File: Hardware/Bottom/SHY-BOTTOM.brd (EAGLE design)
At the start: 160 x 100 mm, 0 parts

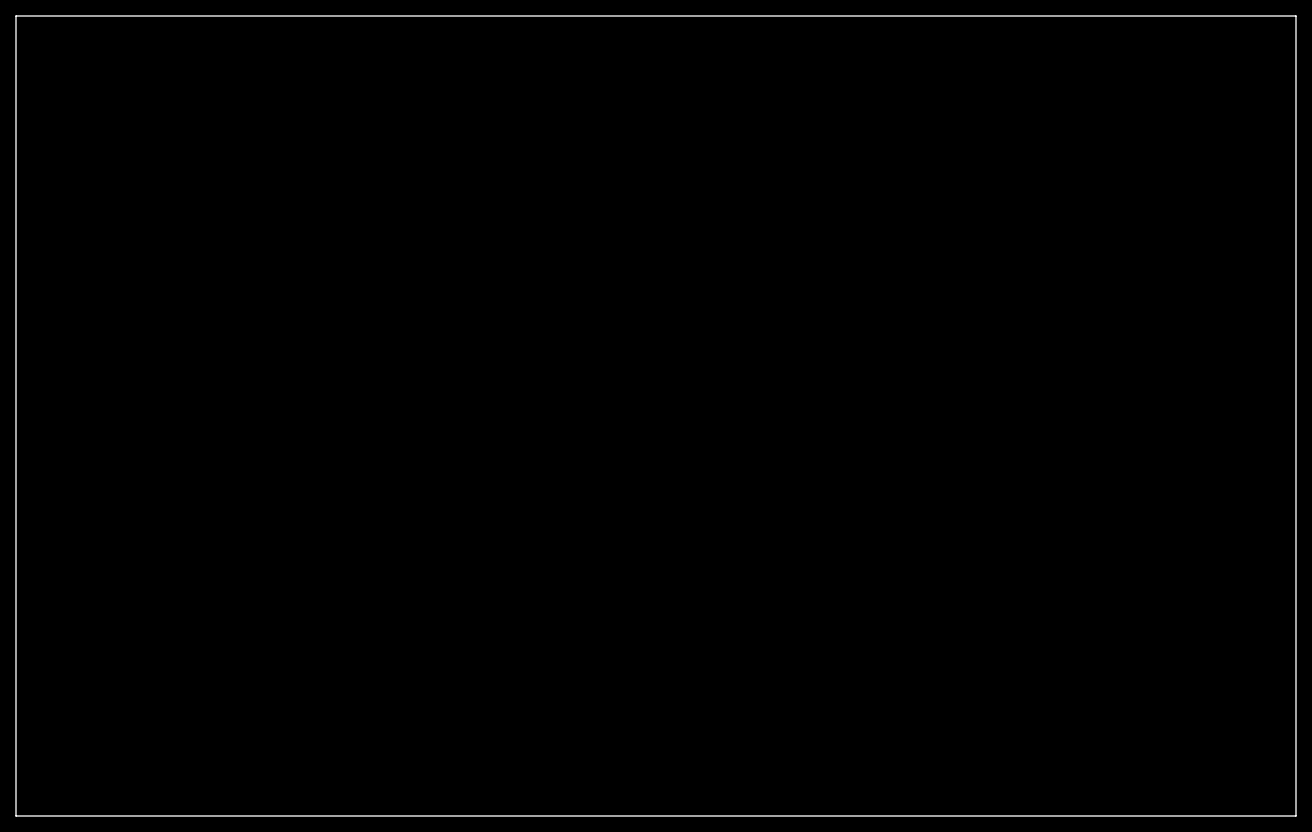
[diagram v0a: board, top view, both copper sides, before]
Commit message: Add content for bottom board
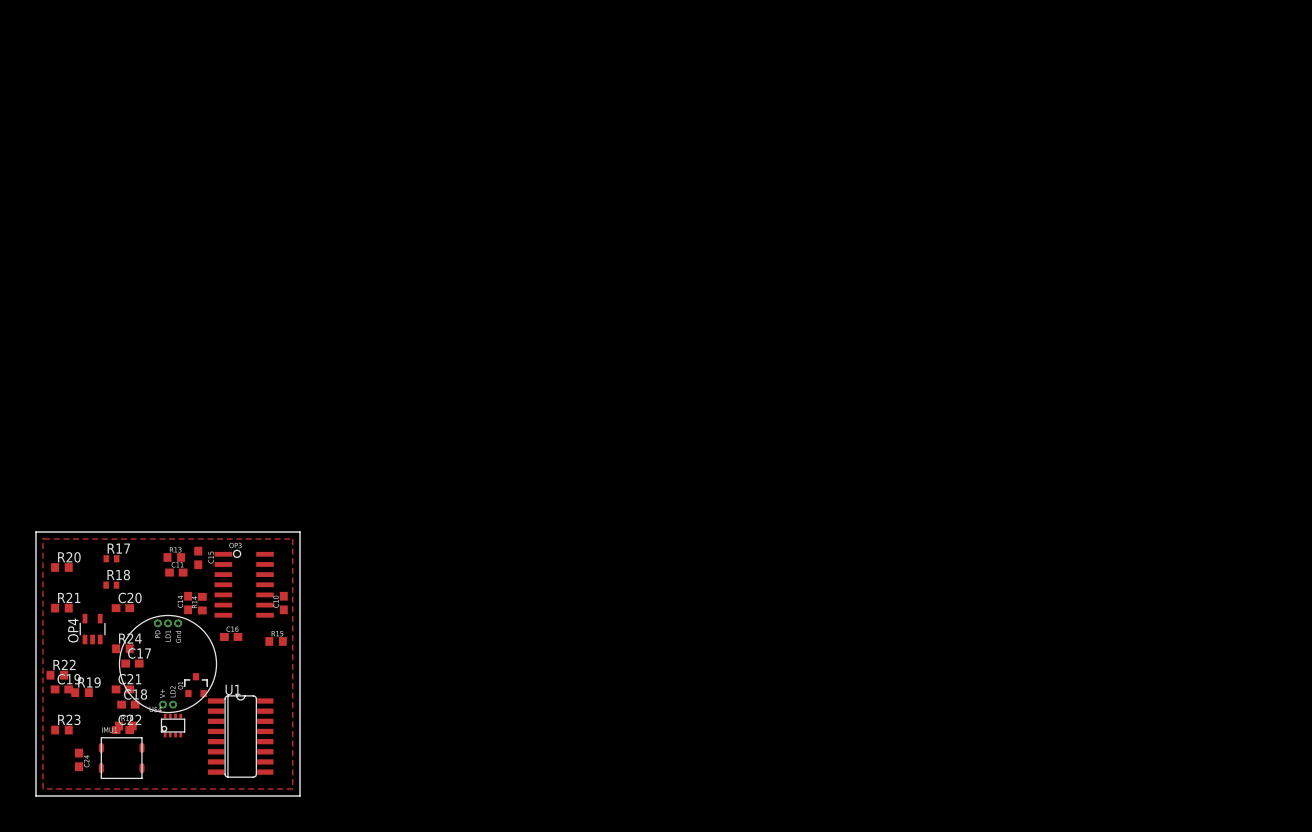
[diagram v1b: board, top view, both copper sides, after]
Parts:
- added C10, C11, C17, C18, C22, C24: 100n, LinnesLab-Passives:C0603
- added C14, C19: 2.2n, LinnesLab-Passives:C0603
- added C15, C16: 2.2u, LinnesLab-Passives:C0603
- added C20: 22u, LinnesLab-Passives:C0603
- added C21: 22n, LinnesLab-Passives:C0603
- added IMU1: LSM6DS3_CAST, LinnesLab-Sensors:LSM6DS3_CAST
- added OP3: (no value), LinnesLab-AnalogIC:SO14
- added OP4: (no value), LinnesLab-AnalogIC:SOT23-5
- added Q1: (no value), LinnesLab-DiscreteSemi:SOT23-3
- added R13, R15, R19, R21: 220k, LinnesLab-Passives:R0603
- added R14, R22: 10M, LinnesLab-Passives:R0603
- added R16: (no value), LinnesLab-Passives:R0603
- added R17, R18: 10k, LinnesLab-Passives:R0402
- added R20, R23: 1M, LinnesLab-Passives:R0603
- added R24: 10k, LinnesLab-Passives:R0603
- added U$3: (no value), LinnesLab-Connectors:PPG.MODULE.2
- added U$4: AD5171, LinnesLab-DigitalIC:SOT-23-8
- added U1: AD5242-SO16, LinnesLab-DigitalIC:SO16
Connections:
- new net 3.3V: C11.2, C17.2, C18.2, C22.2, C24.2, IMU1.2, OP3.4, OP4.5, R13.2, R15.2, R17.2, U$3.V+, U$4.2, U$4.6, U1.5, U1.6
- new net G.A1: U1.2
- new net G.A2: U1.16
- new net G.O1: U1.1
- new net G.O2: U1.13
- new net G.W2: C21.1, OP3.2, R24.1, U1.15
- new net GND: C11.1, C17.1, C18.1, C22.1, C24.1, IMU1.1, OP3.11, OP4.2, OP4.3, Q1.2, R18.1, R19.1, R21.1, U$3.GND, U$4.3, U1.10, U1.11, U1.12, U1.9
- new net LED: Q1.3
- new net LED.C: U$3.LD1
- new net LED.CTRL: U$4.8
- new net N$10: OP3.12, R17.1, R18.2
- new net N$13: C15.2, OP3.5, R13.1, R19.2
- new net N$15: C14.2, OP3.6, R14.1, R20.2
- new net N$16: C14.1, C16.1, OP3.7, R14.2
- new net N$17: C16.2, OP3.10, R15.1, R21.2
- new net N$18: C19.2, OP3.9, R22.1, R23.2
- new net N$19: C19.1, C20.1, OP3.8, R22.2
- new net N$20: C20.2, R24.2
- new net N$8: Q1.1, R16.2
- new net N$9: R16.1, U$4.1, U$4.7
- new net PD.C: C10.1, OP4.4, U$3.PD, U1.4
- new net PPG: C21.2, OP3.1, U1.14
- new net SCL: IMU1.3, U$4.4, U1.7
- new net SDA: IMU1.4, U$4.5, U1.8
- new net TIA: C10.2, C15.1, OP4.1, U1.3
- new net VREF: OP3.13, OP3.14, OP3.3, R20.1, R23.1
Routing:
- added copper zone on layer 1, net 3.3V
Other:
- board size 160 x 100 mm -> 33 x 33 mm

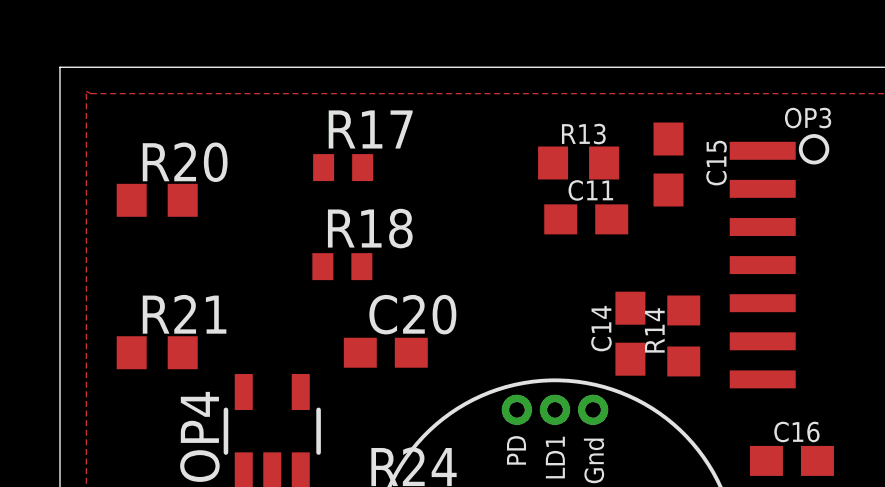
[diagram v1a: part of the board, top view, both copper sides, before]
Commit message: bottom board design
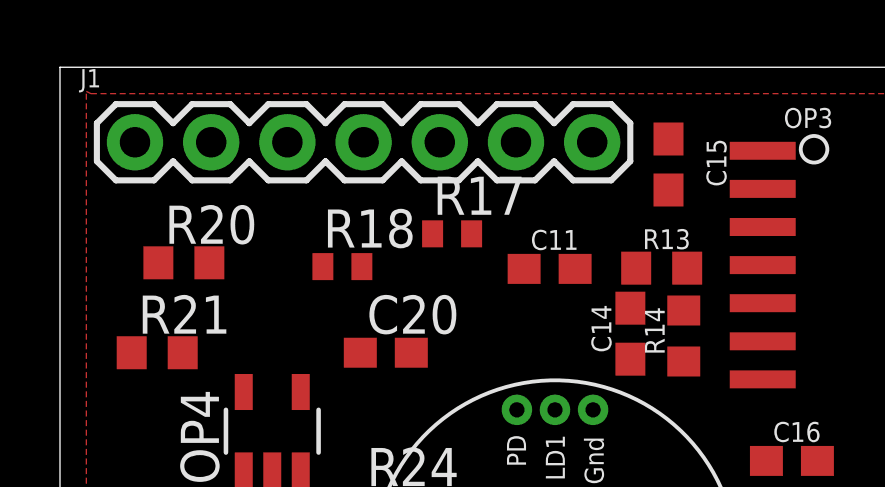
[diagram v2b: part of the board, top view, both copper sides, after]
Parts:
- added J1: (no value), LinnesLab-Connectors:1X07
- moved R13 4.47 mm to (22.6, 28.8)
- moved R17 4.25 mm to (15.6, 29.9)
- moved R20 2.26 mm to (6.63, 29.0)
- moved C11 2.05 mm to (18.8, 28.8)
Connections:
- removed net LED.CTRL: U$4.8
- removed net PPG: C21.2, OP3.1, U1.14
- removed net TIA: C10.2, C15.1, OP4.1, U1.3
- new net A6/TIA: C10.2, C15.1, J1.5, OP4.1, U1.3
- new net A7/PPG: C21.2, J1.7, OP3.1, U1.14
- new net D29/LED.CTRL: J1.6, U$4.8
- new net N$2: J1.4
- new net N$3: J1.3
- new net N$4: J1.2
- new net N$5: J1.1
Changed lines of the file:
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@@
 <setting verticaltext="up"/>
 </settings>
-<grid distance="1" unitdist="mil" unit="mil" style="lines" multiple="1" display="no" altdistance="5" altunitdist="mil" altunit="mil"/>
+<grid distance="1" unitdist="mil" unit="mm" style="lines" multiple="1" display="no" altdistance="5" altunitdist="mil" altunit="mil"/>
 <layers>
 <layer number="1" name="Top" color="4" fill="1" visible="yes" active="yes"/>
@@
 <attribute name="VALUE" x="35.3822" y="25.9842" size="1.27" layer="27" rot="R90"/>
 </element>
-<element name="C11" library="LinnesLab-Passives" package="C0603" value="100n" x="20.0406" y="30.4292" smashed="yes">
-<attribute name="NAME" x="19.4056" y="31.0642" size="0.6604" layer="25"/>
-<attribute name="VALUE" x="19.4056" y="28.5242" size="1.27" layer="27"/>
+<element name="C11" library="LinnesLab-Passives" package="C0603" value="100n" x="18.8214" y="28.7782" smashed="yes">
+<attribute name="NAME" x="18.1864" y="29.4132" size="0.6604" layer="25"/>
+<attribute name="VALUE" x="18.1864" y="26.8732" size="1.27" layer="27"/>
 </element>
 <element name="U$4" library="LinnesLab-DigitalIC" package="SOT-23-8" package3d_urn="urn:adsk.eagle:package:17879439/2" value="AD5171" x="19.6342" y="11.303" smashed="yes">
@@
 <attribute name="VALUE" x="16.7342" y="8.303" size="0.6604" layer="27"/>
 </element>
-<element name="R13" library="LinnesLab-Passives" package="R0603" package3d_urn="urn:adsk.eagle:package:15661944/2" value="220k" x="19.7866" y="32.3088" smashed="yes">
-<attribute name="NAME" x="19.1516" y="32.9438" size="0.6604" layer="25"/>
-<attribute name="VALUE" x="19.1516" y="30.4038" size="1.27" layer="27"/>
+<element name="R13" library="LinnesLab-Passives" package="R0603" package3d_urn="urn:adsk.eagle:package:15661944/2" value="220k" x="22.5552" y="28.8036" smashed="yes">
+<attribute name="NAME" x="21.9202" y="29.4386" size="0.6604" layer="25"/>
+<attribute name="VALUE" x="21.9202" y="26.8986" size="1.27" layer="27"/>
 </element>
 <element name="R14" library="LinnesLab-Passives" package="R0603" package3d_urn="urn:adsk.eagle:package:15661944/2" value="10M" x="23.2918" y="26.543" smashed="yes" rot="R90">
@@
 <attribute name="VALUE" x="26.6192" y="23.0632" size="1.27" layer="27"/>
 </element>
-<element name="R17" library="LinnesLab-Passives" package="R0402" package3d_urn="urn:adsk.eagle:package:15661898/2" value="10k" x="11.938" y="32.1564" smashed="yes">
-<attribute name="NAME" x="11.303" y="32.7914" size="1.27" layer="25"/>
-<attribute name="VALUE" x="11.303" y="30.2514" size="1.27" layer="27"/>
+<element name="R17" library="LinnesLab-Passives" package="R0402" package3d_urn="urn:adsk.eagle:package:15661898/2" value="10k" x="15.5702" y="29.9466" smashed="yes">
+<attribute name="NAME" x="14.9352" y="30.5816" size="1.27" layer="25"/>
+<attribute name="VALUE" x="14.9352" y="28.0416" size="1.27" layer="27"/>
 </element>
 <element name="R18" library="LinnesLab-Passives" package="R0402" package3d_urn="urn:adsk.eagle:package:15661898/2" value="10k" x="11.9126" y="28.8544" smashed="yes">
@@
 <attribute name="VALUE" x="7.62" y="13.5128" size="1.27" layer="27"/>
 </element>
-<element name="R20" library="LinnesLab-Passives" package="R0603" package3d_urn="urn:adsk.eagle:package:15661944/2" value="1M" x="5.7404" y="31.0642" smashed="yes">
-<attribute name="NAME" x="5.1054" y="31.6992" size="1.27" layer="25"/>
-<attribute name="VALUE" x="5.1054" y="29.1592" size="1.27" layer="27"/>
+<element name="R20" library="LinnesLab-Passives" package="R0603" package3d_urn="urn:adsk.eagle:package:15661944/2" value="1M" x="6.6294" y="28.9814" smashed="yes">
+<attribute name="NAME" x="5.9944" y="29.6164" size="1.27" layer="25"/>
+<attribute name="VALUE" x="5.9944" y="27.0764" size="1.27" layer="27"/>
 </element>
 <element name="R21" library="LinnesLab-Passives" package="R0603" package3d_urn="urn:adsk.eagle:package:15661944/2" value="220k" x="5.7404" y="25.9842" smashed="yes">
@@
 <attribute name="NAME" x="8.509" y="7.6454" size="0.6604" layer="25" rot="R270"/>
 <attribute name="VALUE" x="5.969" y="7.6454" size="0.6604" layer="27" rot="R270"/>
+</element>
+<element name="J1" library="LinnesLab-Connectors" package="1X07" value="" x="5" y="33" smashed="yes">
+<attribute name="NAME" x="3.1712" y="34.8288" size="0.6096" layer="25" font="vector" ratio="20"/>
+<attribute name="VALUE" x="3.73" y="30.968" size="0.6096" layer="27" font="vector" ratio="20"/>
 </element>
 </elements>
@@
 <contactref element="C24" pad="1"/>
 <wire x1="20.27" y1="24.08" x2="31.1242" y2="28.9052" width="0" layer="19" extent="1-1"/>
-<wire x1="19.1906" y1="30.4292" x2="20.27" y2="24.08" width="0" layer="19" extent="1-1"/>
-<wire x1="11.2626" y1="28.8544" x2="19.1906" y2="30.4292" width="0" layer="19" extent="1-1"/>
+<wire x1="17.9714" y1="28.7782" x2="20.27" y2="24.08" width="0" layer="19" extent="1-1"/>
+<wire x1="11.2626" y1="28.8544" x2="17.9714" y2="28.7782" width="0" layer="19" extent="1-1"/>
 <wire x1="10.5258" y1="22.062" x2="11.2626" y2="28.8544" width="0" layer="19" extent="1-1"/>
 <wire x1="9.5758" y1="22.062" x2="10.5258" y2="22.062" width="0" layer="19" extent="1-1"/>
@@
 <wire x1="15.748" y1="5.969" x2="20.5936" y2="10.1266" width="0" layer="19" extent="1-1"/>
 </signal>
-<signal name="TIA">
+<signal name="A6/TIA">
 <contactref element="C10" pad="2"/>
 <contactref element="U1" pad="3"/>
 <contactref element="C15" pad="1"/>
 <contactref element="OP4" pad="1"/>
+<contactref element="J1" pad="5"/>
 <wire x1="22.7838" y1="33.108" x2="33.4772" y2="27.4692" width="0" layer="19" extent="1-1"/>
+<wire x1="15.16" y1="33" x2="22.7838" y2="33.108" width="0" layer="19" extent="1-1"/>
+<wire x1="8.6258" y1="22.062" x2="15.16" y2="33" width="0" layer="19" extent="1-1"/>
 <wire x1="25.019" y1="11.8364" x2="33.4772" y2="27.4692" width="0" layer="19" extent="1-1"/>
-<wire x1="8.6258" y1="22.062" x2="22.7838" y2="33.108" width="0" layer="19" extent="1-1"/>
 </signal>
 <signal name="PD.C">
@@
 <wire x1="31.1242" y1="32.7152" x2="31.1242" y2="31.4452" width="0" layer="19" extent="1-1"/>
 <wire x1="25.9242" y1="30.1752" x2="31.1242" y2="31.4452" width="0" layer="19" extent="1-1"/>
-<wire x1="4.8904" y1="31.0642" x2="25.9242" y2="30.1752" width="0" layer="19" extent="1-1"/>
-<wire x1="4.8904" y1="10.7442" x2="4.8904" y2="31.0642" width="0" layer="19" extent="1-1"/>
+<wire x1="5.7794" y1="28.9814" x2="25.9242" y2="30.1752" width="0" layer="19" extent="1-1"/>
+<wire x1="4.8904" y1="10.7442" x2="5.7794" y2="28.9814" width="0" layer="19" extent="1-1"/>
 </signal>
 <signal name="N$9">
@@
 <wire x1="12.8914" y1="11.2522" x2="18.6436" y2="10.1266" width="0" layer="19" extent="1-1"/>
 </signal>
-<signal name="LED.CTRL">
+<signal name="D29/LED.CTRL">
 <contactref element="U$4" pad="8"/>
+<contactref element="J1" pad="6"/>
+<wire x1="18.6436" y1="12.4794" x2="17.7" y2="33" width="0" layer="19" extent="1-1"/>
 </signal>
 <signal name="N$10">
@@
 <contactref element="R18" pad="2"/>
 <wire x1="12.5626" y1="28.8544" x2="31.1242" y2="30.1752" width="0" layer="19" extent="1-1"/>
-<wire x1="11.288" y1="32.1564" x2="12.5626" y2="28.8544" width="0" layer="19" extent="1-1"/>
+<wire x1="14.9202" y1="29.9466" x2="12.5626" y2="28.8544" width="0" layer="19" extent="1-1"/>
 </signal>
 <signal name="LED">
@@
 <contactref element="U1" pad="1"/>
 </signal>
-<signal name="PPG">
+<signal name="A7/PPG">
 <contactref element="U1" pad="14"/>
 <contactref element="C21" pad="2"/>
 <contactref element="OP3" pad="1"/>
-<wire x1="14.2104" y1="15.8242" x2="25.9242" y2="32.7152" width="0" layer="19" extent="1-1"/>
+<contactref element="J1" pad="7"/>
+<wire x1="20.24" y1="33" x2="25.9242" y2="32.7152" width="0" layer="19" extent="1-1"/>
+<wire x1="14.2104" y1="15.8242" x2="20.24" y2="33" width="0" layer="19" extent="1-1"/>
 <wire x1="31.1658" y1="11.8364" x2="14.2104" y2="15.8242" width="0" layer="19" extent="1-1"/>
 </signal>
@@
 <contactref element="R19" pad="2"/>
 <contactref element="OP3" pad="5"/>
-<wire x1="18.9366" y1="32.3088" x2="22.7838" y2="31.408" width="0" layer="19" extent="1-1"/>
+<wire x1="21.7052" y1="28.8036" x2="22.7838" y2="31.408" width="0" layer="19" extent="1-1"/>
 <wire x1="25.9242" y1="27.6352" x2="22.7838" y2="31.408" width="0" layer="19" extent="1-1"/>
-<wire x1="9.105" y1="15.4178" x2="18.9366" y2="32.3088" width="0" layer="19" extent="1-1"/>
+<wire x1="9.105" y1="15.4178" x2="21.7052" y2="28.8036" width="0" layer="19" extent="1-1"/>
 </signal>
 <signal name="N$15">
@@
 <wire x1="23.2918" y1="25.693" x2="25.9242" y2="26.3652" width="0" layer="19" extent="1-1"/>
 <wire x1="21.5138" y1="27.4692" x2="23.2918" y2="25.693" width="0" layer="19" extent="1-1"/>
-<wire x1="6.5904" y1="31.0642" x2="21.5138" y2="27.4692" width="0" layer="19" extent="1-1"/>
+<wire x1="7.4794" y1="28.9814" x2="21.5138" y2="27.4692" width="0" layer="19" extent="1-1"/>
 </signal>
 <signal name="N$16">
@@
 <wire x1="14.2104" y1="20.9042" x2="14.2104" y2="25.9842" width="0" layer="19" extent="1-1"/>
 </signal>
+<signal name="N$2">
+<contactref element="J1" pad="4"/>
+</signal>
+<signal name="N$3">
+<contactref element="J1" pad="3"/>
+</signal>
+<signal name="N$4">
+<contactref element="J1" pad="2"/>
+</signal>
+<signal name="N$5">
+<contactref element="J1" pad="1"/>
+</signal>
 </signals>

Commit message: till 53:17
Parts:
- moved R20 31.7 mm to (28.8, 6.30), turned to 180 degrees
- moved C24 30.2 mm to (25.9, 31.3)
- moved IMU1 30.0 mm to (31.2, 31.2)
- moved C15 28.4 mm to (28.7, 4.49), turned to 0 degrees
- moved R21 26.1 mm to (31.0, 19.5), turned to 270 degrees
- moved R23 25.8 mm to (28.3, 23.3), turned to 180 degrees
- moved R19 25.7 mm to (33.5, 10.7), turned to 270 degrees
- moved R13 24.4 mm to (33.7, 7.09), turned to 270 degrees
- moved C19 23.4 mm to (28.5, 21.2), turned to 180 degrees
- moved R22 23.0 mm to (28.1, 19.6)
- moved C11 20.9 mm to (24.5, 8.63), turned to 90 degrees
- moved C20 20.8 mm to (20.8, 6.58), turned to 270 degrees
- moved C14 20.2 mm to (29.3, 8.01), turned to 180 degrees
- moved C10 19.6 mm to (16.6, 16.6), turned to 180 degrees
- moved R14 18.0 mm to (29.0, 9.42), turned to 0 degrees
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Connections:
- removed net LED: Q1.3
- net LED.C: now also Q1.3
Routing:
- net A6/TIA: track 0.00 -> 36.3 mm, vias 0 -> 2
- net PD.C: track 0.00 -> 26.0 mm, vias 0 -> 2
- net N$19: track 0.00 -> 22.1 mm
- net GND: track 0.00 -> 20.5 mm, vias 0 -> 8
- net A7/PPG: track 0.00 -> 19.5 mm
- net G.W2: track 0.00 -> 16.7 mm, vias 0 -> 2
- net N$17: track 0.00 -> 12.2 mm, vias 0 -> 2
- net N$13: track 0.00 -> 8.17 mm
- net N$18: track 0.00 -> 6.44 mm
- net N$15: track 0.00 -> 6.27 mm
- net N$16: track 0.00 -> 4.54 mm
- net N$10: track 0.00 -> 3.77 mm
- net N$20: track 0.00 -> 2.29 mm
- net VREF: track 0.00 -> 1.27 mm
- net 3.3V: track 0.00 -> 1.00 mm
- added copper zone on layer 16, net GND
